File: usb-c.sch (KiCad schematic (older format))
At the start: 9 parts, among them U1 HD3SS3220

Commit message: First private release.
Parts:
- added C1, C2, C3, C4, C5, C6: 220nF, Capacitor_SMD:C_0603_1608Metric_Pad1.08x0.95mm_HandSolder, symbol Device:C_Small
- added R16, R17: 100K, Resistor_SMD:R_0402_1005Metric_Pad0.72x0.64mm_HandSolder, symbol Device:R_US
- added R18: 1.8M, Resistor_SMD:R_0603_1608Metric_Pad0.98x0.95mm_HandSolder, symbol Device:R_US
- C25: value 1uF -> 470nF
- R12: value 900k -> 1.8M
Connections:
- net +5V: now also R18.2
- net GND: now also R16.2, R17.2
- net RX1+: now also D1.1 (TVS1), D1.10 (NC1), U1.14 (RX1-); no longer D1.2 (TVS2), D1.9 (NC2), U1.15 (RX1+)
- net RX1-: now also D1.2 (TVS2), D1.9 (NC2), U1.15 (RX1+); no longer D1.1 (TVS1), D1.10 (NC1), U1.14 (RX1-)
- net TX+: now also C6.1; no longer U1.7 (TX+)
- net TX-: now also C5.1; no longer U1.6 (TX-)
- net TX1+: now also C2.2; no longer U1.16 (TX1-)
- net TX1-: now also C1.2; no longer U1.17 (TX1+)
- net TX2+: now also D4.5 (TVS4), D4.6 (NC4), C3.2; no longer D4.4 (TVS3), D4.7 (NC3), U1.20 (TX2-)
- net TX2-: now also D4.4 (TVS3), D4.7 (NC3), C4.2; no longer D4.5 (TVS4), D4.6 (NC4), U1.21 (TX2+)
- net at R12.1, U1.5 (VBUS_DET): now also R18.1
- net at R14.1: now also U1.11 (DIR); no longer U1.27 (ID)
- new net TX1_AC+: C2.1, U1.16 (TX1-)
- new net TX1_AC-: C1.1, U1.17 (TX1+)
- new net TX2_AC+: C4.1, U1.20 (TX2-)
- new net TX2_AC-: C3.1, U1.21 (TX2+)
- new net TX_MUX_DC+: C6.2, R17.1, U1.7 (TX+)
- new net TX_MUX_DC-: C5.2, R16.1, U1.6 (TX-)
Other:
- moved on the sheet: C12, C25, D1, D4, D5, R12, R13, R14, U1

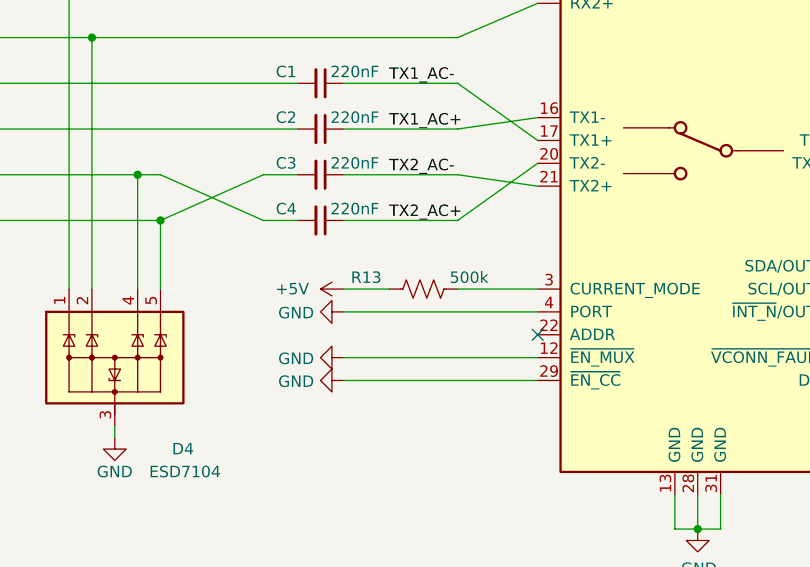
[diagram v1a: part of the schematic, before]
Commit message: Change R13 to a no-connection item
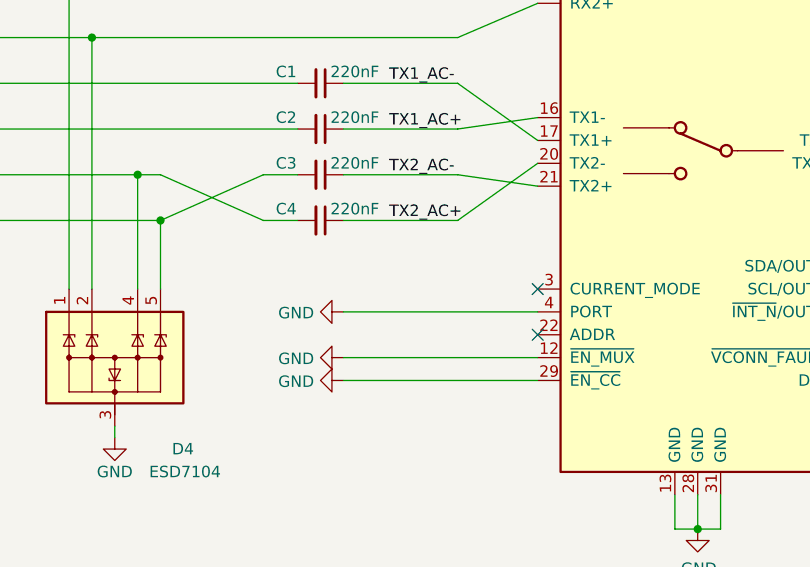
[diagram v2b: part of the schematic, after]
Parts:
- removed R13: 500k, Resistor_SMD:R_0603_1608Metric_Pad0.98x0.95mm_HandSolder, symbol Device:R_US
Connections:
- no-connect marks 6 -> 7
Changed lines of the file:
@@
 	5000 4700 5450 4500
 Connection ~ 5000 4700
-Wire Wire Line
-	6300 5000 6650 5000
-$Comp
-L power:+5V #PWR0149
-U 1 1 60A82DCB
-P 5800 5000
-F 0 "#PWR0149" H 5800 4850 50  0001 C CNN
-F 1 "+5V" V 5800 5150 50  0000 L CNN
-F 2 "" H 5800 5000 50  0001 C CNN
-F 3 "" H 5800 5000 50  0001 C CNN
-	1    5800 5000
-	0    -1   -1   0
-$EndComp
-Wire Wire Line
-	5800 5000 6000 5000
-$Comp
-L Device:R_US R13
-U 1 1 5FD29CF3
-P 6150 5000
-F 0 "R13" V 6100 4750 50  0000 C CNN
-F 1 "500k" V 6100 5200 50  0000 C CNN
-F 2 "Resistor_SMD:R_0603_1608Metric_Pad0.98x0.95mm_HandSolder" V 6190 4990 50  0001 C CNN
-F 3 "~" H 6150 5000 50  0001 C CNN
-	1    6150 5000
-	0    1    1    0
-$EndComp
+NoConn ~ 6650 5000
 $EndSCHEMATC

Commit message: various changes for v0.01 public release.
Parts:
- added R13: NC, Resistor_SMD:R_0603_1608Metric_Pad0.98x0.95mm_HandSolder, symbol Device:R_US
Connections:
- net GND: now also R13.1, R13.2
- net TX2_AC+: now also C3.1, U1.21 (TX2+); no longer C4.1, U1.20 (TX2-)
- net TX2_AC-: now also C4.1, U1.20 (TX2-); no longer C3.1, U1.21 (TX2+)
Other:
- note added: "Note on TX-/TX+"
- note added: "The common-mode DC\non RX and TX lines must\nbe less than 2 V, but VL670\nhas up to 2.2 V DC at TX\nlines (RX lines are okay).\n\nThus, we need to block\nDC by C5 and C6, then\nuse R16 and R17 to re-\nbias the operating point\nto 0 V.\n\nC1/2/3/4 are always needed\nto block DC at the host. C5/6\nand R16/17 are only needed\nwhen common-mode DC is\ngreater than 2 V, like VL670.\n\nUse 0402 or small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"
- note added: "originally for HD3SS3320,\nnow deleted but keep it on\n board for stencil reuse.\n\nas a good practice, floating\ncopper pads grounded.\n\nyou can use them as\nprobe grounding points."
- moved on the sheet: C1, C12, C2, C25, C3, C4, C5, C6, D1, D4, D5, R12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

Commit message: v0.02.
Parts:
- removed R13: NC, Resistor_SMD:R_0603_1608Metric_Pad0.98x0.95mm_HandSolder, symbol Device:R_US
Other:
- note removed: "originally for HD3SS3320,\nnow deleted but keep it on\n board for stencil reuse.\n\nas a good practice, floating\ncopper pads grounded.\n\nyou can use them as\nprobe grounding points."
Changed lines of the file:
@@
 encoding utf-8
 Sheet 2 4
-Title "USB-C Schematic - VL670 Development Board"
-Date "2021-06-29"
-Rev "v0.01"
+Title "USB-C Schematic - VL670/671 Development Board"
+Date "2021-10-26"
+Rev "v0.02"
 Comp "Copyright (C) 2021 Tom Li (niconiconi)"
 Comment1 "https://creativecommons.org/publicdomain/zero/1.0/"
@@
 Wire Notes Line
 	9050 5500 10800 5500
-$Comp
-L power:GND #PWR?
-U 1 1 60DD4114
-P 5050 6800
-AR Path="/60C6101E/60DD4114" Ref="#PWR?"  Part="1"
-AR Path="/60085564/60DD4114" Ref="#PWR0149"  Part="1"
-F 0 "#PWR0149" H 5050 6550 50  0001 C CNN
-F 1 "GND" H 5055 6627 50  0000 C CNN
-F 2 "" H 5050 6800 50  0001 C CNN
-F 3 "" H 5050 6800 50  0001 C CNN
-	1    5050 6800
-	1    0    0    -1
-$EndComp
-Wire Wire Line
-	4900 6600 5050 6800
-Wire Wire Line
-	5200 6600 5050 6800
-Connection ~ 5050 6800
-Text Notes 3450 7100 0    50   ~ 0
-originally for HD3SS3320,\nnow deleted but keep it on\n board for stencil reuse.\n\nas a good practice, floating\ncopper pads grounded.\n\nyou can use them as\nprobe grounding points.
-$Comp
-L Device:R_US R13
-U 1 1 60DD411E
-P 5050 6600
-AR Path="/60085564/60DD411E" Ref="R13"  Part="1"
-AR Path="/60C6101E/60DD411E" Ref="R?"  Part="1"
-F 0 "R13" V 5000 6350 50  0000 C CNN
-F 1 "NC" V 5000 6800 50  0000 C CNN
-F 2 "Resistor_SMD:R_0603_1608Metric_Pad0.98x0.95mm_HandSolder" V 5090 6590 50  0001 C CNN
-F 3 "~" H 5050 6600 50  0001 C CNN
-	1    5050 6600
-	0    1    1    0
-$EndComp
 $EndSCHEMATC

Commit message: usb-b edition
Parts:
- removed C1, C2: 220nF, Capacitor_SMD:C_0603_1608Metric_Pad1.08x0.95mm_HandSolder, symbol Device:C_Small
- removed C12: 1uF, Capacitor_SMD:C_0603_1608Metric_Pad1.08x0.95mm_HandSolder, symbol Device:C
- removed C25: 470nF, Capacitor_SMD:C_0603_1608Metric_Pad1.08x0.95mm_HandSolder, symbol Device:C
- removed D1, D4: ESD7104, vl670:OnSemi_UDFN-10_1.0x2.5mm_P0.5mm, symbol vl670:ESD7104
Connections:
- wire segments 95 -> 81
